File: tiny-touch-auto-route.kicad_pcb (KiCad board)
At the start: 2 copper layers, 100.3 x 76 mm, 122 parts, among them IC1 STM32F072VBT6, Q1 DTC123J, SW1 SW_Push, U1 MCP1700-3002E_SOT23, U2 SRV05-4

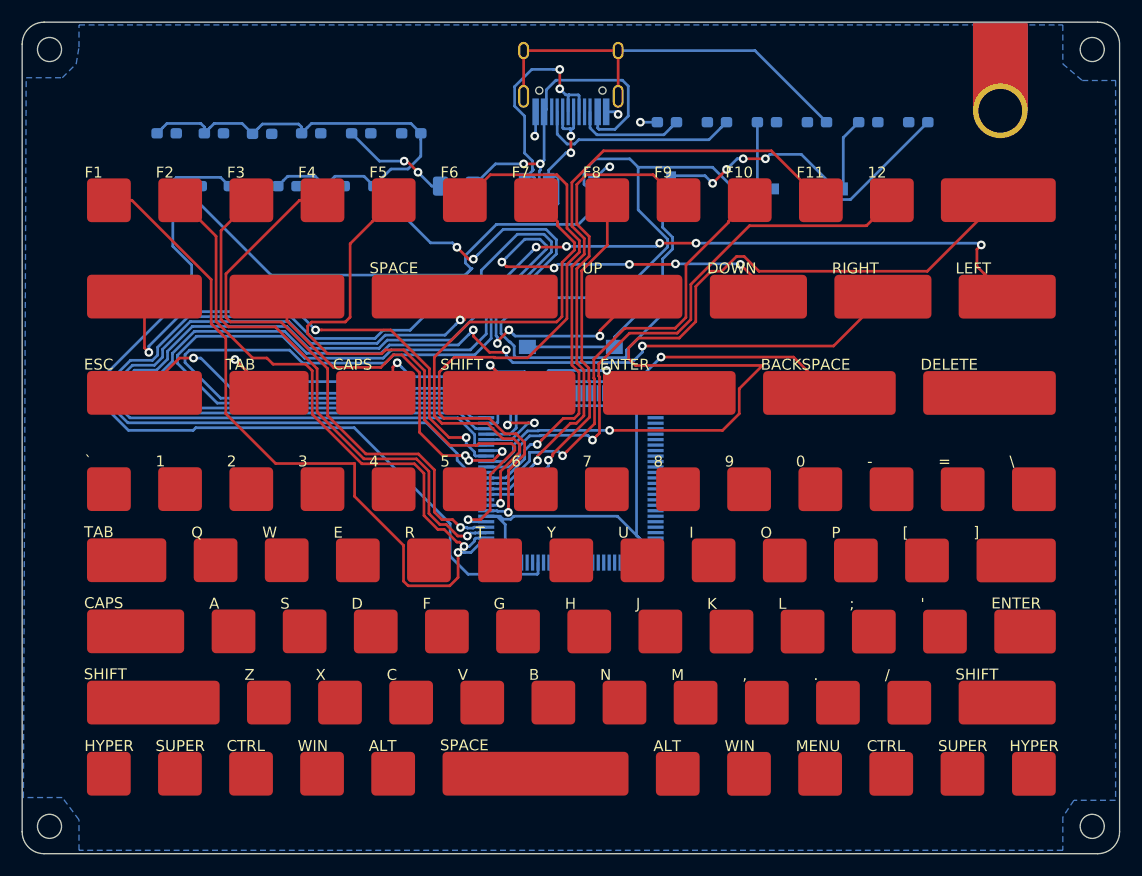
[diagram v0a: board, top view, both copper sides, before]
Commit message: Try to add more traces
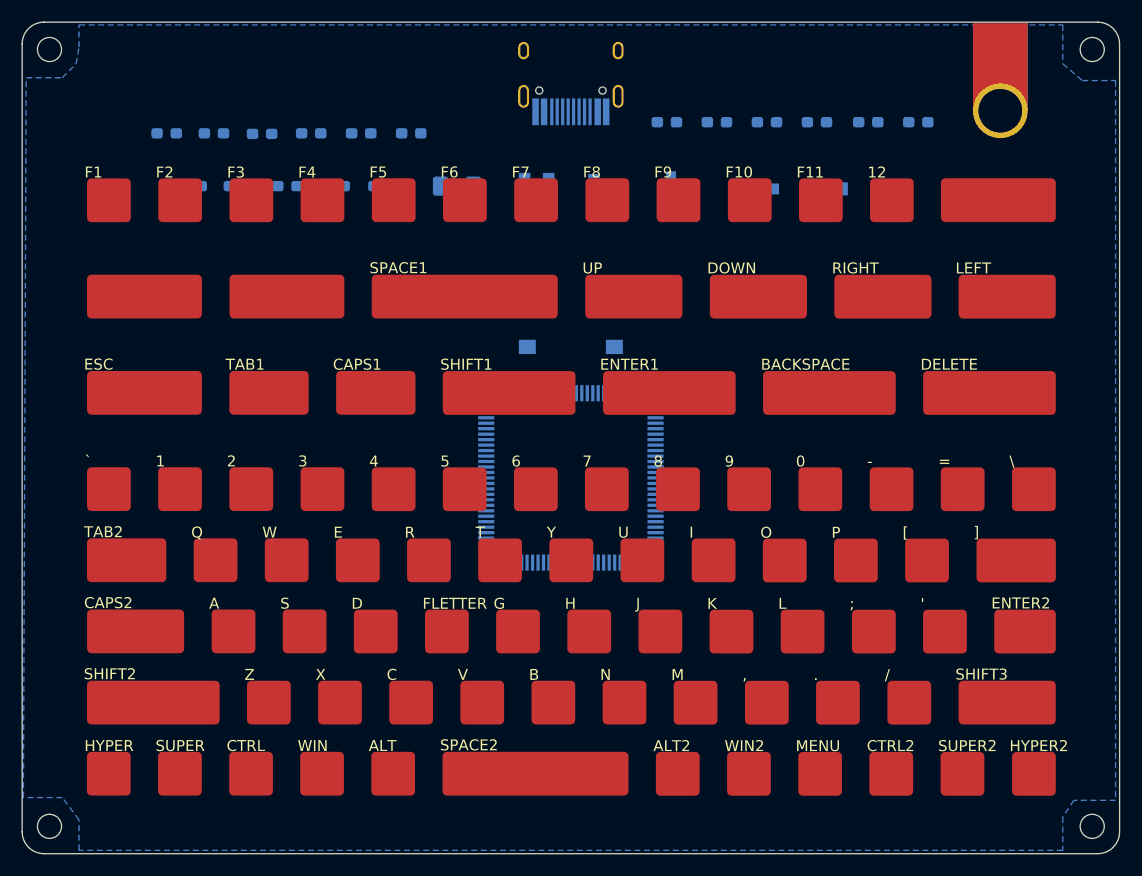
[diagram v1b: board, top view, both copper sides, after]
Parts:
- renumbered ALT to ALT2, CAPS to CAPS1, CAPS to CAPS2, CTRL to CTRL2, ENTER to ENTER1, ENTER to ENTER2, F to FLETTER, HYPER to HYPER2, SHIFT to SHIFT1, SHIFT to SHIFT2, SHIFT to SHIFT3, SPACE to SPACE1, SPACE to SPACE2, SUPER to SUPER2, TAB to TAB1, TAB to TAB2, WIN to WIN2
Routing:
- net +3V3: track 196.9 -> 0.00 mm, vias 6 -> 0
- net NRST: track 127.0 -> 0.00 mm
- net A2: track 118.3 -> 0.00 mm, vias 5 -> 0
- net A1: track 113.1 -> 0.00 mm, vias 3 -> 0
- net F3: track 112.0 -> 0.00 mm, vias 3 -> 0
- net A0: track 104.6 -> 0.00 mm, vias 5 -> 0
- net C1: track 86.5 -> 0.00 mm, vias 1 -> 0
- net BOOTO: track 86.1 -> 0.00 mm
- net F2: track 76.3 -> 0.00 mm, vias 1 -> 0
- net E2: track 62.1 -> 0.00 mm, vias 1 -> 0
- net F1: track 59.5 -> 0.00 mm, vias 1 -> 0
- net C13: track 59.4 -> 0.00 mm, vias 1 -> 0
- net E6: track 54.4 -> 0.00 mm, vias 1 -> 0
- net C0: track 53.8 -> 0.00 mm, vias 1 -> 0
- net E5: track 52.2 -> 0.00 mm, vias 1 -> 0
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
